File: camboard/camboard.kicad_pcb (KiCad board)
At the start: 2 copper layers, 76.2 x 76.2 mm, 61 parts, among them J1 USB_microB_2040002-1, J2 Micro_SD_Card, J3 PPTC102LFBN-RC, J4 Conn_ARM_JTAG_SWD_20, J5 GS2, J6 Conn_01x25_Female, J7 Conn_01x25_Female, SW1 SW_DPDT_x2, SW2 SW_Push, SW3 SW_Push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

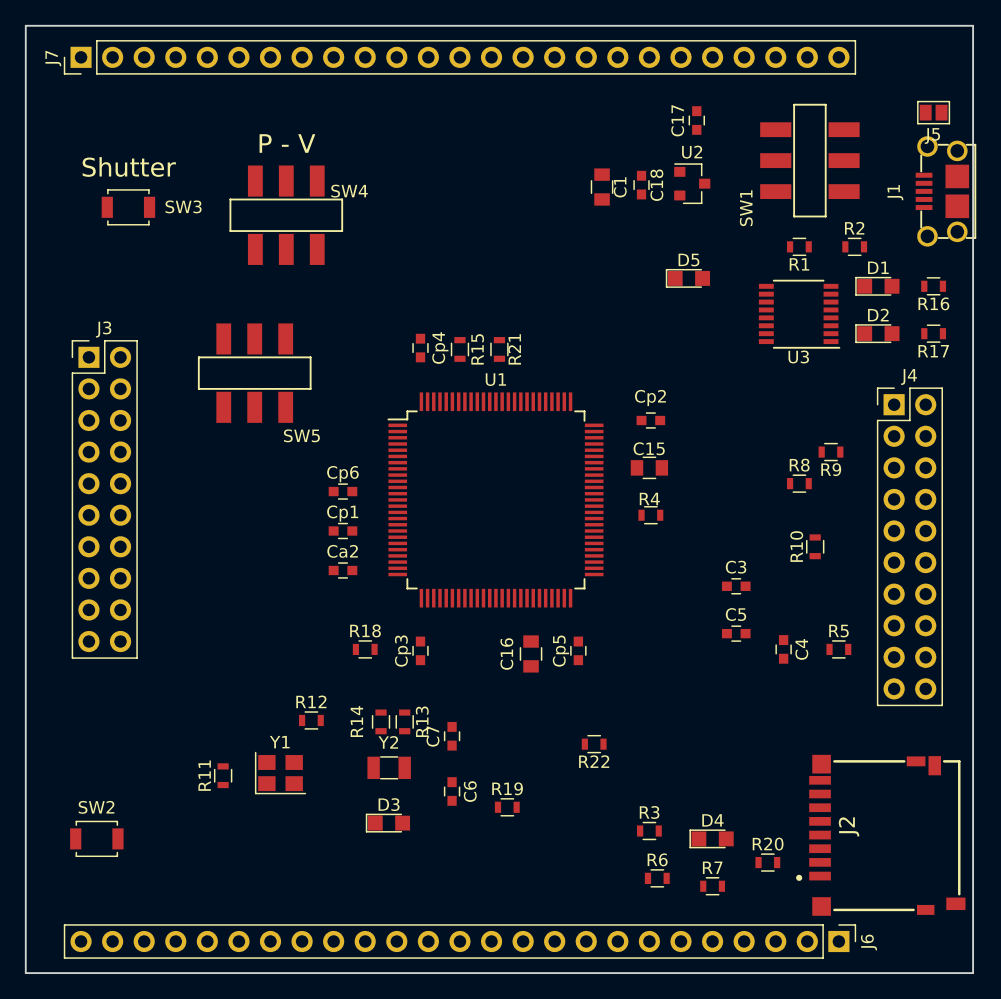
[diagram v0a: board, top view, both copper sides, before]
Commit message: Manual pre-routing of power
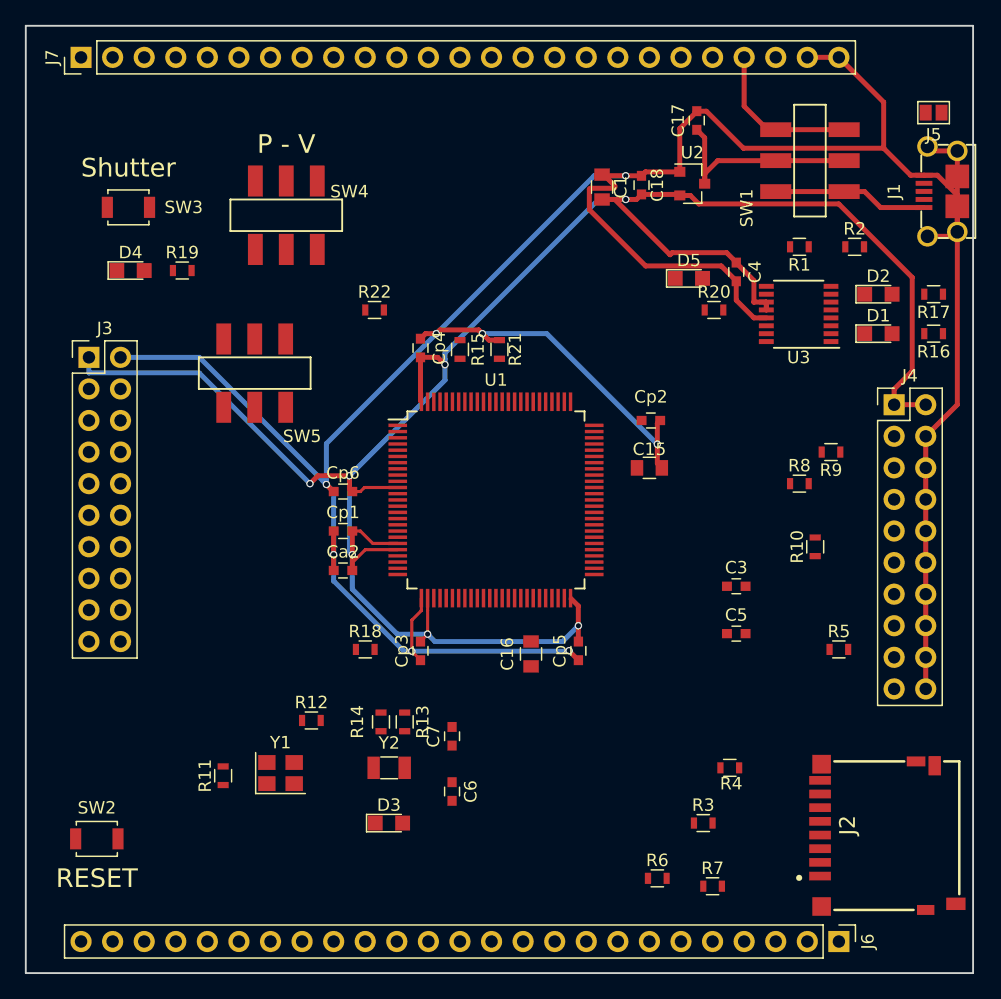
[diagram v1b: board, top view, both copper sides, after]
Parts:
- moved D4 65.4 mm to (46.5, 57.8)
- moved R19 50.5 mm to (50.7, 57.8)
- moved R20 44.7 mm to (93.5, 61.0)
- moved R22 39.1 mm to (66.2, 61.0), turned to 0 degrees
- moved C4 30.6 mm to (95.2, 57.9)
- moved R4 21.3 mm to (94.7, 97.8), turned to 0 degrees
- moved R3 4.38 mm to (92.6, 102.2)
- moved D1 3.81 mm to (106.7, 62.9)
- moved R16 3.81 mm to (111.1, 62.9)
- moved D2 3.18 mm to (106.7, 59.7)
- moved R17 3.18 mm to (111.1, 59.7)
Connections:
- J3 pad 17: Net-(J3-Pad17) -> (no net)
- J3 pad 18: Net-(J3-Pad18) -> (no net)
- J6 pad 1: GND -> (no net)
- J6 pad 2: +3V3 -> (no net)
- J6 pad 3: /VIN -> (no net)
- U1 pad 13: Net-(U1-Pad13) -> (no net)
- U1 pad 6: Net-(U1-Pad6) -> (no net)
- U1 pad 63: Net-(U1-Pad63) -> (no net)
- U1 pad 64: Net-(U1-Pad64) -> (no net)
- U1 pad 87: Net-(U1-Pad87) -> (no net)
- U1 pad 91: Net-(U1-Pad91) -> (no net)
- U1 pad 92: Net-(U1-Pad92) -> (no net)
- U1 pad 95: Net-(U1-Pad95) -> (no net)
- U1 pad 96: Net-(U1-Pad96) -> (no net)
- U3 pad 10: Net-(U3-Pad10) -> (no net)
- U3 pad 15: Net-(U3-Pad15) -> (no net)
- U3 pad 16: Net-(U3-Pad16) -> (no net)
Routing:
- net GND: track 0.00 -> 249.2 mm, vias 0 -> 8
- net +3V3: track 0.00 -> 179.2 mm, vias 0 -> 7
- net Net-(C17-Pad1): track 0.00 -> 17.0 mm
- net /VIN: track 0.00 -> 12.8 mm
- net /USB_5V: track 0.00 -> 12.5 mm
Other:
- board text added: "RESET"

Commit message: The ladybug is happy
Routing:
- net GND: track 249.2 -> 473.1 mm, vias 8 -> 9
- net +3V3: track 179.2 -> 372.7 mm, vias 7 -> 9
- net /NRST: track 0.00 -> 138.4 mm, vias 0 -> 1
- net Net-(J6-Pad24): track 0.00 -> 111.0 mm, vias 0 -> 2
- net /DCMI_D1: track 0.00 -> 108.3 mm, vias 0 -> 3
- net /DCMI_D0: track 0.00 -> 104.6 mm, vias 0 -> 3
- net Net-(J6-Pad23): track 0.00 -> 89.4 mm, vias 0 -> 1
- net Net-(J7-Pad3): track 0.00 -> 87.0 mm, vias 0 -> 2
- net /CLK: track 0.00 -> 86.8 mm, vias 0 -> 2
- net Net-(J7-Pad17): track 0.00 -> 83.5 mm, vias 0 -> 1
- net Net-(J4-Pad13): track 0.00 -> 81.6 mm, vias 0 -> 1
- net Net-(J7-Pad18): track 0.00 -> 81.4 mm, vias 0 -> 2
- net Net-(J7-Pad12): track 0.00 -> 78.6 mm, vias 0 -> 1
- net /DCMI_D5: track 0.00 -> 72.7 mm, vias 0 -> 1
- net Net-(J7-Pad20): track 0.00 -> 71.4 mm, vias 0 -> 1
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
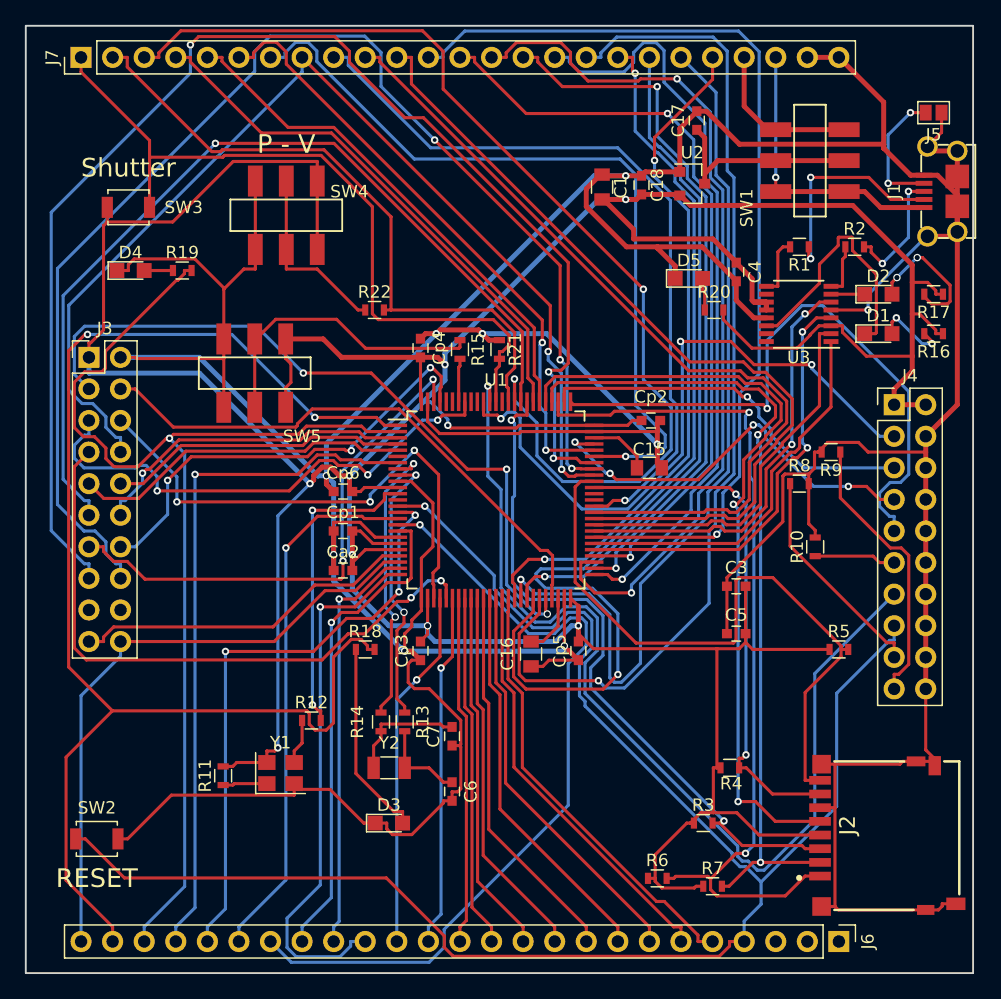
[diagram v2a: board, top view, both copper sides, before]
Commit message: Moved SD card and processor
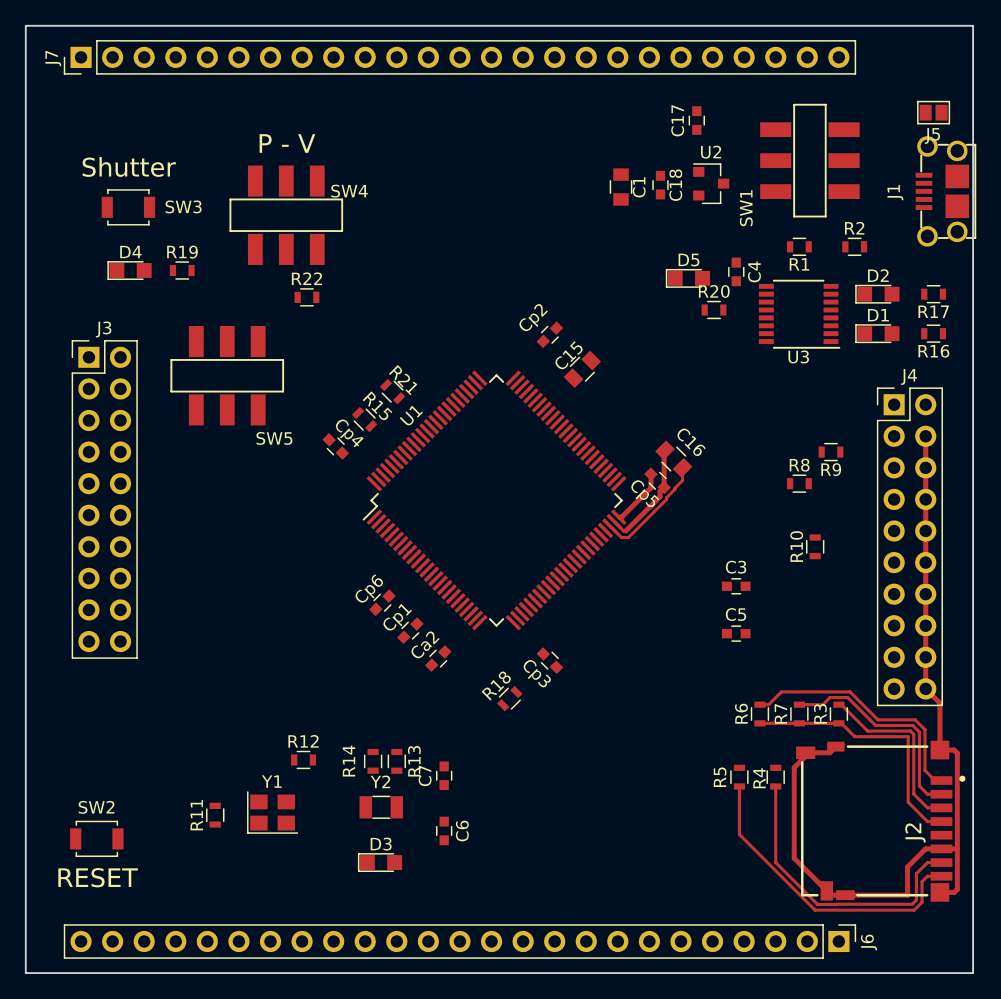
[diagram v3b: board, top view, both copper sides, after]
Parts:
- moved C16 19.4 mm to (90.2, 73.0), turned to 135 degrees
- moved R6 15.6 mm to (97.2, 93.5), turned to 90 degrees
- moved R7 15.5 mm to (100.3, 93.5), turned to 90 degrees
- moved Cp5 15.1 mm to (88.9, 74.7), turned to 135 degrees
- moved J2 15.0 mm to (103.3, 96.1), turned to 90 degrees
- moved R3 14.0 mm to (103.5, 93.5), turned to 90 degrees
- moved R5 13.0 mm to (95.5, 98.5), turned to 270 degrees
- moved R18 12.3 mm to (77.0, 92.2), turned to 45 degrees
- moved Cp2 10.7 mm to (80.3, 63.0), turned to 225 degrees
- moved Cp4 10.4 mm to (63.0, 71.9), turned to 315 degrees
- moved Cp3 10.4 mm to (80.3, 89.2), turned to 135 degrees
- moved Ca2 10.4 mm to (71.3, 89.0), turned to 45 degrees
- moved Cp1 9.67 mm to (69.0, 86.8), turned to 45 degrees
- moved C15 9.59 mm to (82.9, 65.7), turned to 45 degrees
- moved R15 9.51 mm to (65.4, 69.8), turned to 315 degrees
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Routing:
- net GND: track 473.1 -> 77.8 mm, vias 9 -> 0
- net +3V3: track 372.7 -> 25.6 mm, vias 9 -> 0
- net /NRST: track 138.4 -> 0.00 mm, vias 1 -> 0
- net Net-(J6-Pad24): track 111.0 -> 0.00 mm, vias 2 -> 0
- net /DCMI_D1: track 108.3 -> 0.00 mm, vias 3 -> 0
- net /DCMI_D0: track 104.6 -> 0.00 mm, vias 3 -> 0
- net Net-(J6-Pad23): track 89.4 -> 0.00 mm, vias 1 -> 0
- net Net-(J7-Pad3): track 87.0 -> 0.00 mm, vias 2 -> 0
- net /CLK: track 86.8 -> 0.00 mm, vias 2 -> 0
- net Net-(J7-Pad17): track 83.5 -> 0.00 mm, vias 1 -> 0
- net Net-(J4-Pad13): track 81.6 -> 0.00 mm, vias 1 -> 0
- net Net-(J7-Pad18): track 81.4 -> 0.00 mm, vias 2 -> 0
- net Net-(J7-Pad12): track 78.6 -> 0.00 mm, vias 1 -> 0
- net /DCMI_D5: track 72.7 -> 0.00 mm, vias 1 -> 0
- net Net-(J7-Pad20): track 71.4 -> 0.00 mm, vias 1 -> 0
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
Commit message: Kept moving parts
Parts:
- removed C3: 1uF, Capacitors_SMD:C_0603
- moved C5 40.2 mm to (59.2, 104.6), turned to 180 degrees
- moved R21 29.4 mm to (45.2, 48.5), turned to 270 degrees
- moved R9 17.1 mm to (101.3, 89.4)
- moved R22 13.9 mm to (54.1, 47.8)
- moved R8 11.5 mm to (101.4, 86.4), turned to 180 degrees
- moved R19 5.47 mm to (45.2, 57.6), turned to 270 degrees
- moved SW4 5.08 mm to (54.0, 53.3)
- moved SW3 4.91 mm to (42.7, 49.5), turned to 90 degrees
- moved D4 3.86 mm to (42.7, 57.5), turned to 90 degrees
- moved R10 3.31 mm to (101.3, 83.3), turned to 180 degrees
- moved R11 0.57 mm to (53.8, 101.3)
- moved Ca2 0.20 mm to (71.1, 88.9)
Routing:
- net Net-(J7-Pad1): track 0.00 -> 49.0 mm
- net Net-(J7-Pad2): track 0.00 -> 42.5 mm
- net GND: track 77.8 -> 106.0 mm
- net Net-(R15-Pad1): track 0.00 -> 20.2 mm
- net +3V3: track 25.6 -> 41.9 mm
- net Net-(R22-Pad1): track 0.00 -> 8.60 mm

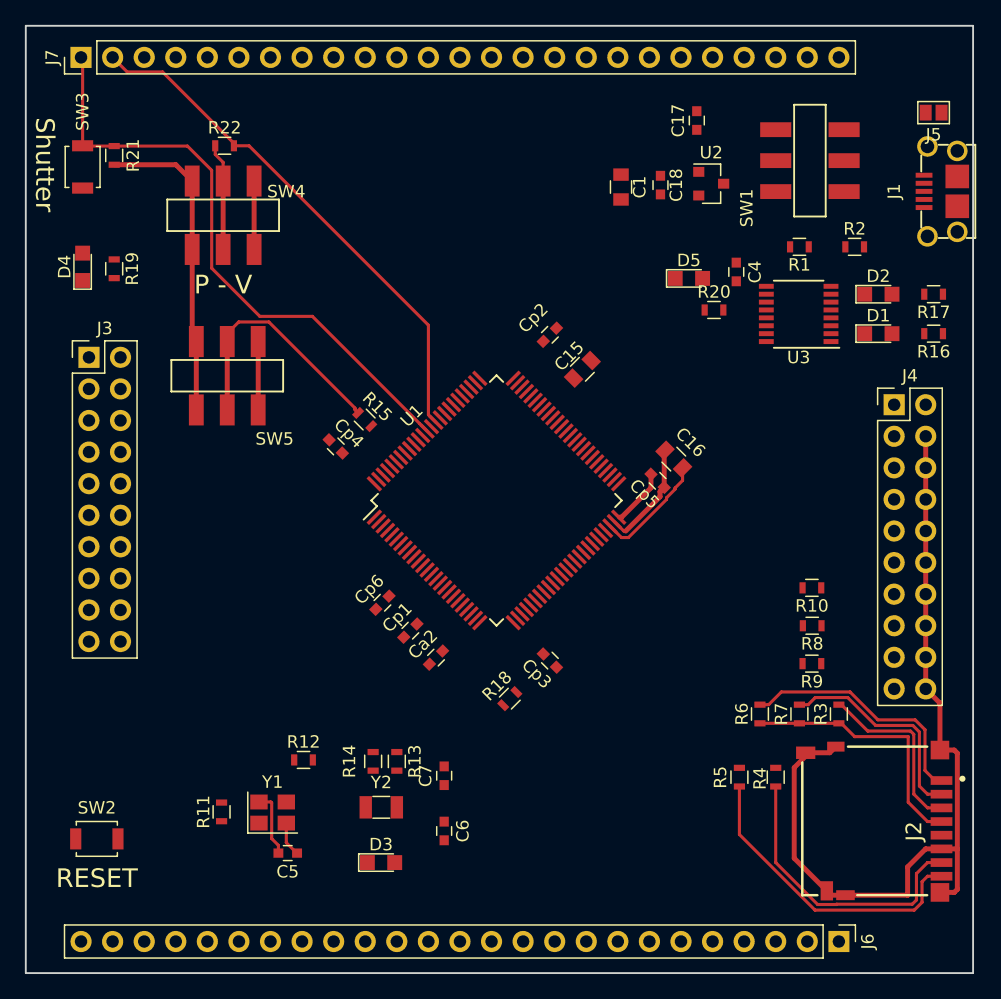
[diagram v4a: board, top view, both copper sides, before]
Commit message: More power traces and cam clock
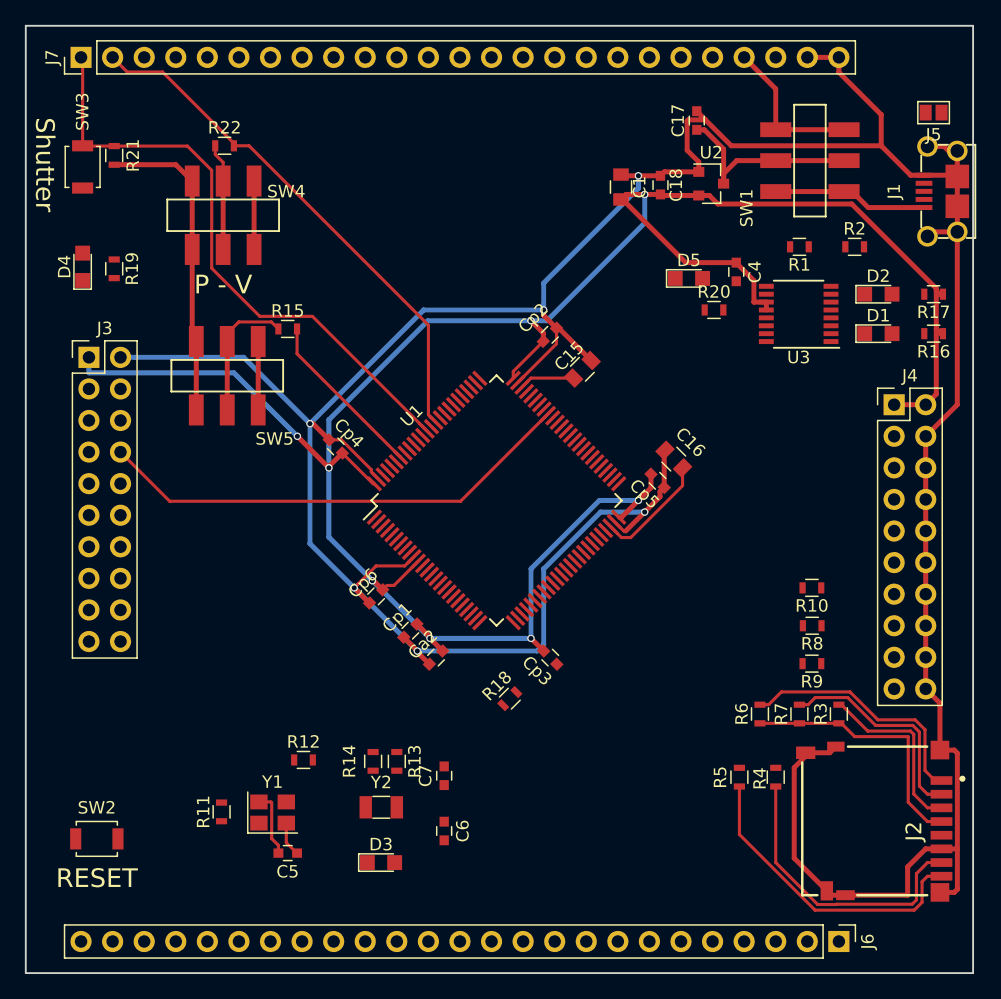
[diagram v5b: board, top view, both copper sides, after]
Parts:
- moved R15 9.56 mm to (59.2, 62.5), turned to 0 degrees
- moved Cp6 0.72 mm to (66.3, 84.0)
- moved Cp3 0.24 mm to (80.3, 88.9)
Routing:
- net GND: track 106.0 -> 313.2 mm, vias 0 -> 6
- net +3V3: track 41.9 -> 225.2 mm, vias 0 -> 8
- net /CLK: track 0.00 -> 39.0 mm
- net Net-(C17-Pad1): track 0.00 -> 16.5 mm
- net Net-(R15-Pad2): track 0.00 -> 13.8 mm
- net /USB_5V: track 0.00 -> 12.5 mm
- net /VIN: track 0.00 -> 12.4 mm
- net Net-(R15-Pad1): track 20.2 -> 10.9 mm
- net Net-(C15-Pad1): track 0.00 -> 4.45 mm

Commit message: Moved some more components
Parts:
- moved R19 31.1 mm to (57.1, 86.4), turned to 0 degrees
- moved D4 30.8 mm to (53.3, 86.4), turned to 0 degrees
- moved D3 25.9 mm to (53.3, 83.3)
- moved R18 21.8 mm to (57.2, 83.3), turned to 0 degrees
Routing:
- net /DCMI_D1: track 0.00 -> 66.3 mm
- net /DCMI_D0: track 0.00 -> 56.3 mm
- net Net-(J7-Pad21): track 0.00 -> 55.5 mm
- net Net-(J7-Pad20): track 0.00 -> 53.2 mm
- net Net-(J7-Pad19): track 0.00 -> 50.9 mm
- net Net-(J7-Pad18): track 0.00 -> 49.7 mm
- net Net-(J7-Pad17): track 0.00 -> 48.4 mm
- net Net-(J6-Pad15): track 0.00 -> 33.9 mm
- net /DCMI_D4: track 0.00 -> 33.3 mm
- net /DCMI_D7: track 0.00 -> 26.6 mm
- net /DCMI_D6: track 0.00 -> 23.5 mm
- net GND: track 313.2 -> 309.6 mm
- net Net-(D5-Pad2): track 0.00 -> 2.61 mm
- net +3V3: track 225.2 -> 226.1 mm
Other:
- net class Default: clearance 0.2 -> 0.1524; trace_width 0.25 -> 0.1524; via_dia 0.6 -> 0.5842; via_drill 0.4 -> 0.381
- rule trace_clearance: 0.2 -> 0.1524
- rule trace_min: 0.2 -> 0.1524
- rule via_min_drill: 0.3 -> 0.381
- rule via_min_size: 0.4 -> 0.5842
